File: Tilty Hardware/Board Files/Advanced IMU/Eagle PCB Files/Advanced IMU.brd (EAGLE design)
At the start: 38.1 x 50.8 mm, 13 parts, among them U3 MPL3115A2LGA8, U6 HMC5883LSMD

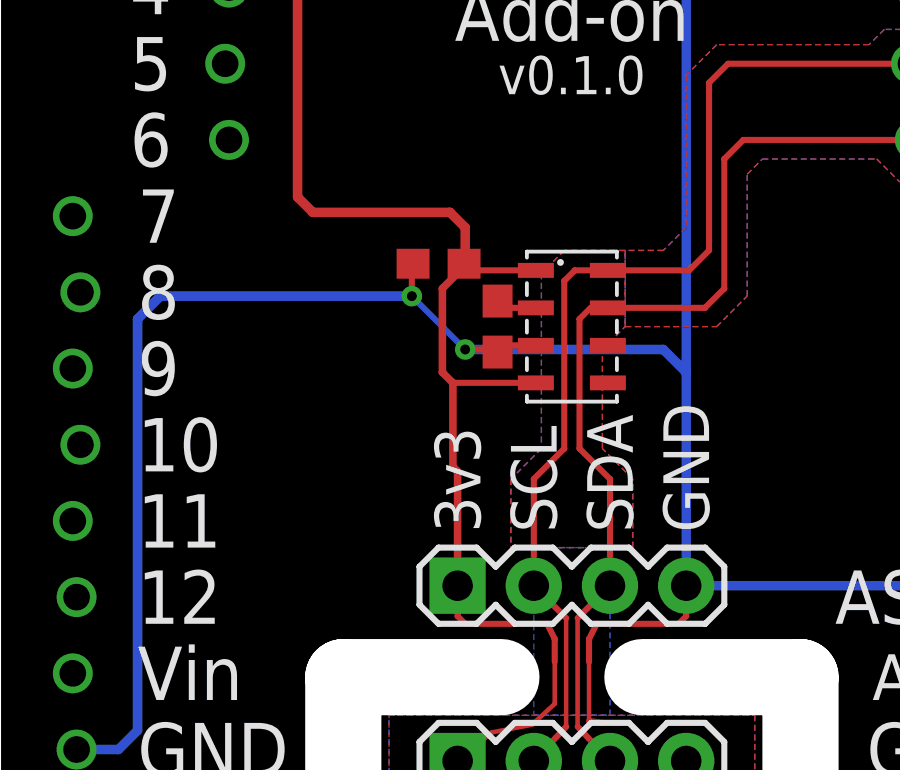
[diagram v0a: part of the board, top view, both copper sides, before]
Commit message: Minor changes
Added current limit resistor to zener shunt on Tilty Duo/Quad.
Added power supply solder jumper to Advanced IMU altimeter.
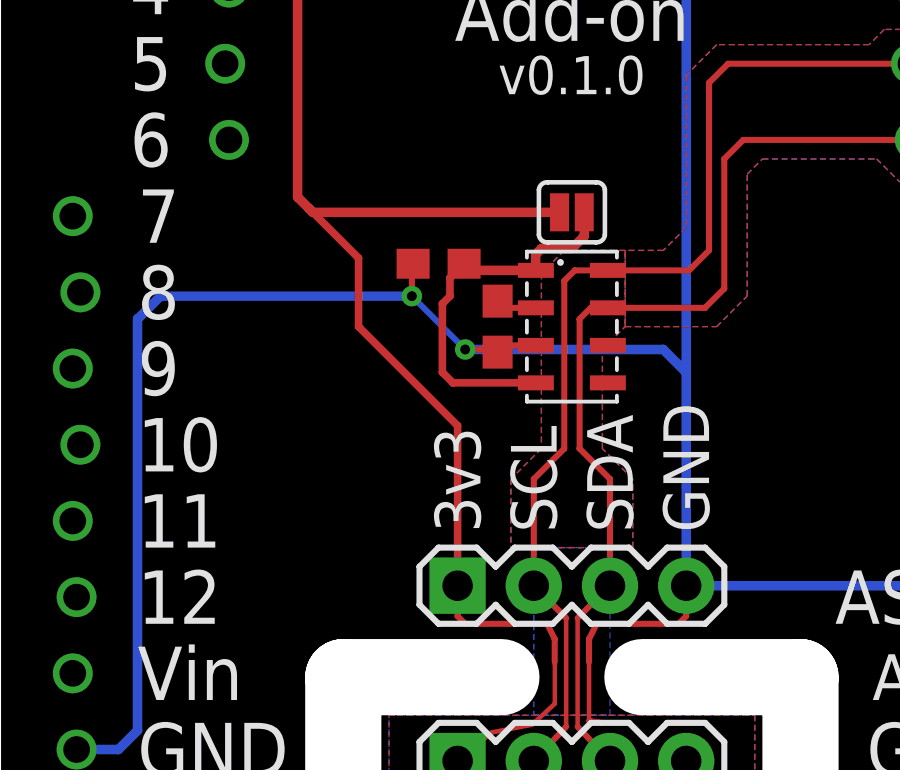
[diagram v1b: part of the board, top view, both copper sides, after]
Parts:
- added SJ1: SOLDERJUMPERNC, SparkFun-Passives:SJ_2S
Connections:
- new net N$3: C12.2, SJ1.1, U3.1, U3.4
- net +3V3: now also SJ1.2; no longer C12.2, U3.1, U3.4
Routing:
- net N$3: track 0.00 -> 12.9 mm
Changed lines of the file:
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@@
 <attribute name="VALUE" x="13.97" y="13.589" size="1.27" layer="27"/>
+</element>
+<element name="SJ1" library="SparkFun-Passives" package="SJ_2S" value="SOLDERJUMPERNC" x="19.05" y="29.21" smashed="yes" rot="R180">
+<attribute name="VALUE" x="19.9998" y="30.861" size="0.4064" layer="27" rot="R180"/>
 </element>
 </elements>
@@
 <contactref element="U6" pad="2"/>
 <contactref element="C6" pad="1"/>
-<contactref element="U3" pad="1"/>
-<contactref element="U3" pad="4"/>
-<contactref element="C12" pad="2"/>
 <contactref element="JP5" pad="1"/>
 <contactref element="JP6" pad="1"/>
@@
 <wire x1="17.014" y1="8.005" x2="17.014" y2="4.568" width="0.2032" layer="16"/>
 <wire x1="17.014" y1="4.568" x2="16.51" y2="4.064" width="0.2032" layer="16"/>
-<wire x1="17.85" y1="27.275" x2="15.6755" y2="27.275" width="0.2032" layer="1"/>
-<wire x1="15.6755" y1="27.275" x2="15.455" y2="27.4955" width="0.2032" layer="1"/>
-<wire x1="17.85" y1="23.525" x2="15.083" y2="23.525" width="0.2032" layer="1"/>
 <wire x1="7.493" y1="49.403" x2="9.271" y2="49.403" width="0.3175" layer="1"/>
 <wire x1="9.271" y1="49.403" x2="9.906" y2="48.768" width="0.3175" layer="1"/>
 <wire x1="9.906" y1="48.768" x2="9.906" y2="29.718" width="0.3175" layer="1"/>
-<wire x1="9.906" y1="29.718" x2="10.414" y2="29.21" width="0.3175" layer="1"/>
-<wire x1="10.414" y1="29.21" x2="14.986" y2="29.21" width="0.3175" layer="1"/>
-<wire x1="14.986" y1="29.21" x2="15.494" y2="28.702" width="0.3175" layer="1"/>
-<wire x1="15.494" y1="28.702" x2="15.494" y2="27.5345" width="0.3175" layer="1"/>
-<wire x1="15.494" y1="27.5345" x2="15.455" y2="27.4955" width="0.3175" layer="1"/>
-<wire x1="15.455" y1="27.4955" x2="15.455" y2="27.393" width="0.254" layer="1"/>
-<wire x1="15.455" y1="27.393" x2="14.732" y2="26.67" width="0.254" layer="1"/>
-<wire x1="14.732" y1="26.67" x2="14.732" y2="23.876" width="0.254" layer="1"/>
-<wire x1="14.732" y1="23.876" x2="15.083" y2="23.525" width="0.254" layer="1"/>
-<wire x1="15.083" y1="23.525" x2="15.083" y2="20.731" width="0.254" layer="1"/>
-<wire x1="15.083" y1="20.731" x2="15.24" y2="20.574" width="0.254" layer="1"/>
-<wire x1="15.24" y1="20.574" x2="15.24" y2="16.764" width="0.254" layer="1"/>
+<wire x1="9.906" y1="29.718" x2="10.287" y2="29.337" width="0.3175" layer="1"/>
+<wire x1="10.287" y1="29.337" x2="10.414" y2="29.21" width="0.3175" layer="1"/>
+<wire x1="10.414" y1="29.21" x2="18.6381" y2="29.21" width="0.3175" layer="1"/>
+<wire x1="15.24" y1="22.098" x2="15.24" y2="16.764" width="0.254" layer="1"/>
 <wire x1="15.24" y1="16.764" x2="15.24" y2="15.748" width="0.2032" layer="1"/>
 <wire x1="15.24" y1="15.748" x2="15.494" y2="15.494" width="0.2032" layer="1"/>
@@
 <wire x1="17.7165" y1="12.1285" x2="16.383" y2="11.8745" width="0.1524" layer="1"/>
 <wire x1="16.383" y1="11.8745" x2="15.24" y2="10.922" width="0.1524" layer="1"/>
+<contactref element="SJ1" pad="2"/>
+<wire x1="15.24" y1="22.098" x2="11.938" y2="25.4" width="0.254" layer="1"/>
+<wire x1="11.938" y1="25.4" x2="11.938" y2="27.686" width="0.254" layer="1"/>
+<wire x1="11.938" y1="27.686" x2="10.287" y2="29.337" width="0.254" layer="1"/>
 </signal>
 <signal name="+5V">
@@
 <wire x1="16.735" y1="26.025" x2="16.5735" y2="26.25" width="0.2032" layer="1"/>
 </signal>
+<signal name="N$3">
+<contactref element="U3" pad="1"/>
+<contactref element="U3" pad="4"/>
+<contactref element="C12" pad="2"/>
+<contactref element="SJ1" pad="1"/>
+<wire x1="19.4619" y1="29.21" x2="19.4619" y2="28.4154" width="0.3175" layer="1"/>
+<wire x1="19.4619" y1="28.4154" x2="19.05" y2="28.0035" width="0.3175" layer="1"/>
+<wire x1="19.05" y1="28.0035" x2="18.034" y2="28.0035" width="0.3175" layer="1"/>
+<wire x1="18.034" y1="28.0035" x2="17.8435" y2="27.813" width="0.3175" layer="1"/>
+<wire x1="17.8435" y1="27.813" x2="17.8435" y2="27.2815" width="0.3175" layer="1"/>
+<wire x1="17.8435" y1="27.2815" x2="17.85" y2="27.275" width="0.3175" layer="1"/>
+<wire x1="17.85" y1="27.275" x2="15.6755" y2="27.275" width="0.3175" layer="1"/>
+<wire x1="15.6755" y1="27.275" x2="15.455" y2="27.4955" width="0.3175" layer="1"/>
+<wire x1="17.85" y1="23.525" x2="15.083" y2="23.525" width="0.254" layer="1"/>
+<wire x1="15.083" y1="23.525" x2="14.732" y2="23.876" width="0.254" layer="1"/>
+<wire x1="14.732" y1="23.876" x2="14.732" y2="26.162" width="0.254" layer="1"/>
+<wire x1="14.732" y1="26.162" x2="14.986" y2="26.416" width="0.254" layer="1"/>
+<wire x1="14.986" y1="26.416" x2="14.986" y2="27.0265" width="0.254" layer="1"/>
+<wire x1="14.986" y1="27.0265" x2="15.455" y2="27.4955" width="0.254" layer="1"/>
+</signal>
 </signals>
